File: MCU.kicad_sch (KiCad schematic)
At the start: 0 parts

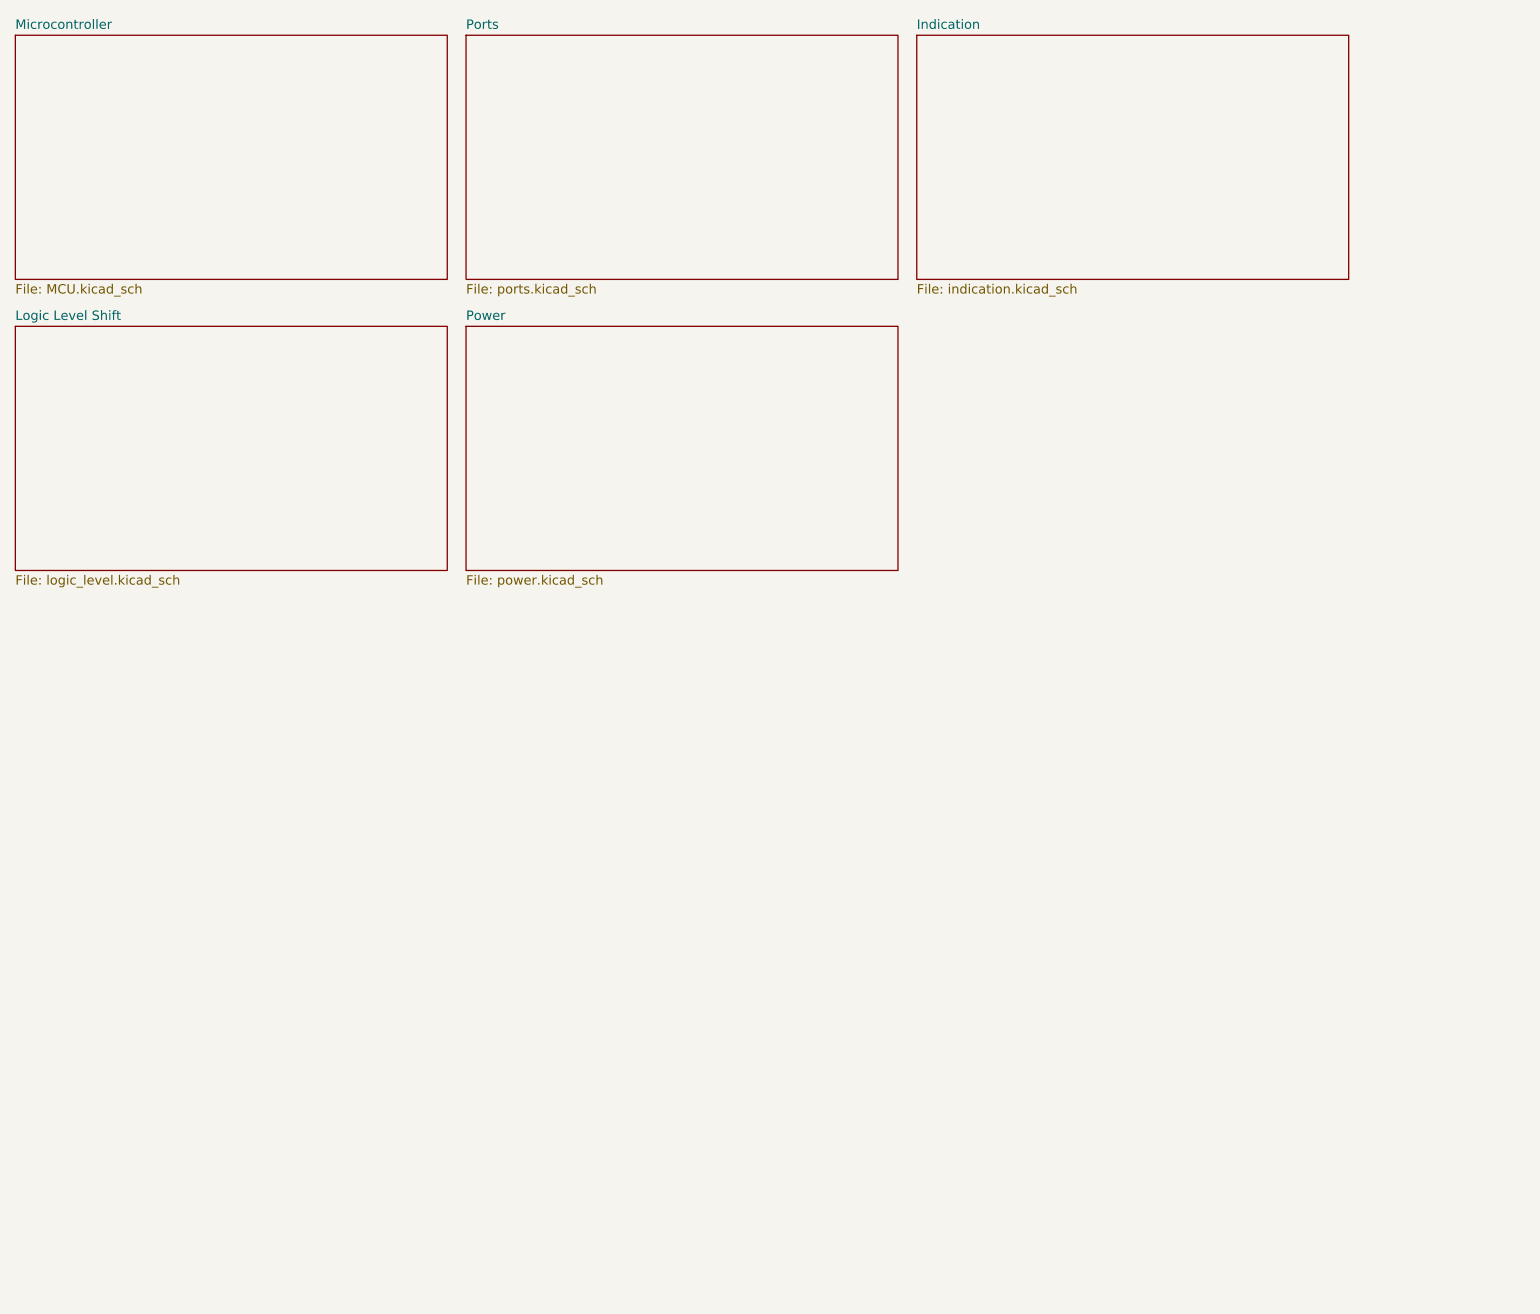
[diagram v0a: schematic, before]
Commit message: Break up schematic into hierarchical sheets
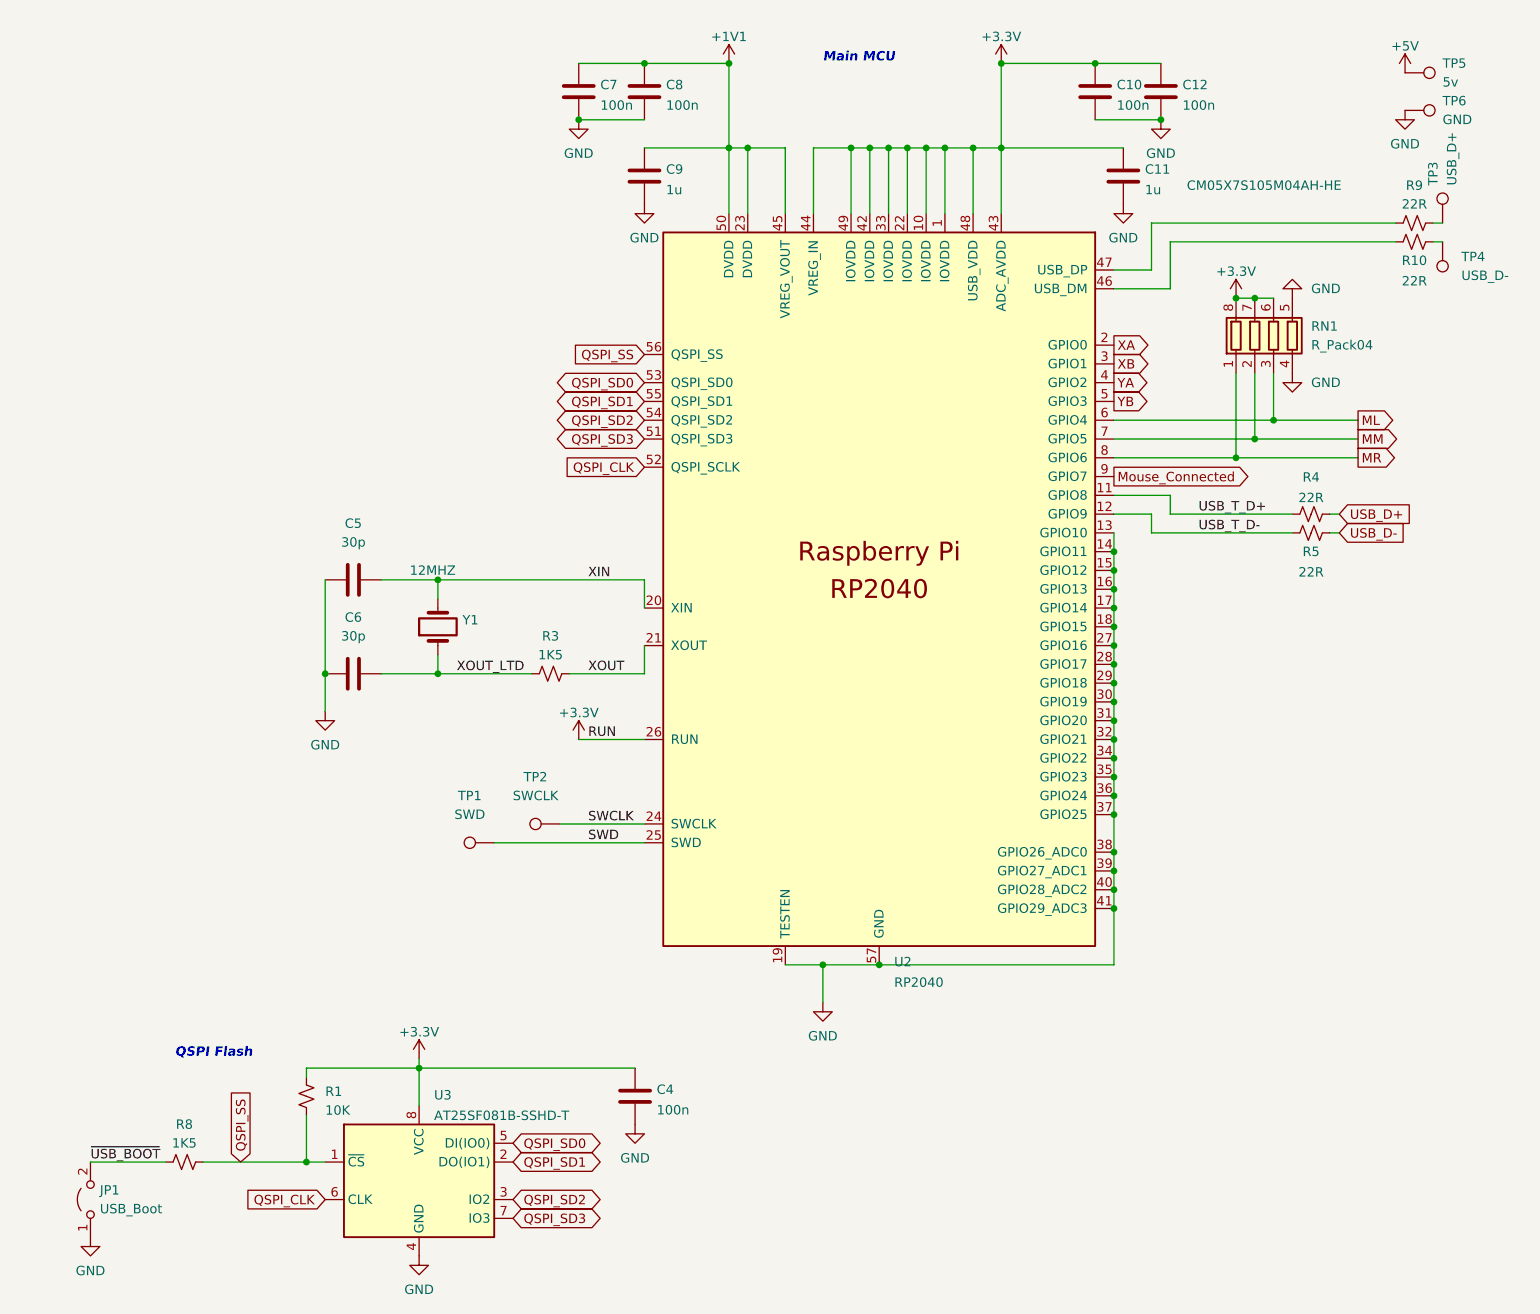
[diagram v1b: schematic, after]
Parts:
- added C10, C12, C4, C7, C8: 100n, Capacitor_SMD:C_0402_1005Metric, symbol Device:C
- added C11, C9: 1u, Capacitor_SMD:C_0402_1005Metric, symbol Device:C
- added C5, C6: 30p, Capacitor_SMD:C_0402_1005Metric, symbol Device:C
- added JP1: USB_Boot, Connector_PinHeader_1.27mm:PinHeader_1x02_P1.27mm_Vertical, symbol Jumper:Jumper_2_Open
- added R1: 10K, Resistor_SMD:R_0402_1005Metric, symbol Device:R_Small_US
- added R10, R4, R5, R9: 22R, Resistor_SMD:R_0402_1005Metric, symbol Device:R_Small_US
- added R3, R8: 1K5, Resistor_SMD:R_0402_1005Metric, symbol Device:R_Small_US
- added RN1: R_Pack04, Resistor_SMD:R_Array_Concave_4x0402, symbol Device:R_Pack04
- added TP1: SWD, TestPoint:TestPoint_Pad_D1.0mm, symbol Connector:TestPoint
- added TP2: SWCLK, TestPoint:TestPoint_Pad_D1.0mm, symbol Connector:TestPoint
- added TP3: USB_D+, TestPoint:TestPoint_Pad_D1.0mm, symbol Connector:TestPoint
- added TP4: USB_D-, TestPoint:TestPoint_Pad_D1.0mm, symbol Connector:TestPoint
- added TP5: 5v, TestPoint:TestPoint_Pad_D1.0mm, symbol Connector:TestPoint
- added TP6: GND, TestPoint:TestPoint_Pad_D1.0mm, symbol Connector:TestPoint
- added U2: RP2040, Library:RP2040-QFN-56, symbol RP2040:RP2040
- added U3: AT25SF081B-SSHD-T, Package_SO:SOIC-8-1EP_3.9x4.9mm_P1.27mm_EP2.29x3mm, symbol Memory_Flash:W25Q32JVZP
- added Y1: 12MHZ, Crystal:Crystal_SMD_5032-2Pin_5.0x3.2mm, symbol Device:Crystal
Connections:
- new net: R10.1, TP4.1
- new net: R10.2, U2.46 (USB_DM)
- new net: R9.2, TP3.1
- new net: R9.1, U2.47 (USB_DP)
- new net +1V1: C7.1, C8.1, C9.1, U2.23 (DVDD), U2.45 (VREG_VOUT), U2.50 (DVDD)
- new net +3V3: C10.1, C11.1, C12.1, C4.1, R1.1, RN1.6 (R3.2), RN1.7 (R2.2), RN1.8 (R1.2), U2.1 (IOVDD), U2.10 (IOVDD), U2.22 (IOVDD), U2.26 (RUN), U2.33 (IOVDD), U2.42 (IOVDD), U2.43 (ADC_AVDD), U2.44 (VREG_IN), U2.48 (USB_VDD), U2.49 (IOVDD), U3.8 (VCC)
- new net +5V: TP5.1
- new net GND: C10.2, C11.2, C12.2, C4.2, C5.1, C6.1, C7.2, C8.2, C9.2, JP1.1 (A), RN1.4 (R4.1), RN1.5 (R4.2), TP6.1, U2.13 (GPIO10), U2.14 (GPIO11), U2.15 (GPIO12), U2.16 (GPIO13), U2.17 (GPIO14), U2.18 (GPIO15), U2.19 (TESTEN), U2.27 (GPIO16), U2.28 (GPIO17), U2.29 (GPIO18), U2.30 (GPIO19), U2.31 (GPIO20), U2.32 (GPIO21), U2.34 (GPIO22), U2.35 (GPIO23), U2.36 (GPIO24), U2.37 (GPIO25), U2.38 (GPIO26_ADC0), U2.39 (GPIO27_ADC1), U2.40 (GPIO28_ADC2), U2.41 (GPIO29_ADC3), U2.57 (GND), U3.4 (GND)
- new net ML: RN1.3 (R3.1), U2.6 (GPIO4)
- new net MM: RN1.2 (R2.1), U2.7 (GPIO5)
- new net MR: RN1.1 (R1.1), U2.8 (GPIO6)
- new net Mouse_Connected: U2.9 (GPIO7)
- new net QSPI_CLK: U2.52 (QSPI_SCLK), U3.6 (CLK)
- new net QSPI_SD0: U2.53 (QSPI_SD0), U3.5 (DI(IO0))
- new net QSPI_SD1: U2.55 (QSPI_SD1), U3.2 (DO(IO1))
- new net QSPI_SD2: U2.54 (QSPI_SD2), U3.3 (IO2)
- new net QSPI_SD3: U2.51 (QSPI_SD3), U3.7 (IO3)
- new net QSPI_SS: R1.2, R8.2, U2.56 (QSPI_SS), U3.1 (~{CS})
- new net SWCLK: TP2.1, U2.24 (SWCLK)
- new net SWD: TP1.1, U2.25 (SWD)
- new net USB_D+: R4.2
- new net USB_D-: R5.1
- new net USB_T_D+: R4.1, U2.11 (GPIO8)
- new net USB_T_D-: R5.2, U2.12 (GPIO9)
- new net XA: U2.2 (GPIO0)
- new net XB: U2.3 (GPIO1)
- new net XIN: C5.2, U2.20 (XIN), Y1.2
- new net XOUT: R3.2, U2.21 (XOUT)
- new net XOUT_LTD: C6.2, R3.1, Y1.1
- new net YA: U2.4 (GPIO2)
- new net YB: U2.5 (GPIO3)
- new net ~{USB_BOOT}: JP1.2 (B), R8.1
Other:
- removed sheet Indication
- removed sheet Logic Level Shift
- removed sheet Microcontroller
- removed sheet Ports
- removed sheet Power
- note added: "Main MCU"
- note added: "QSPI Flash"

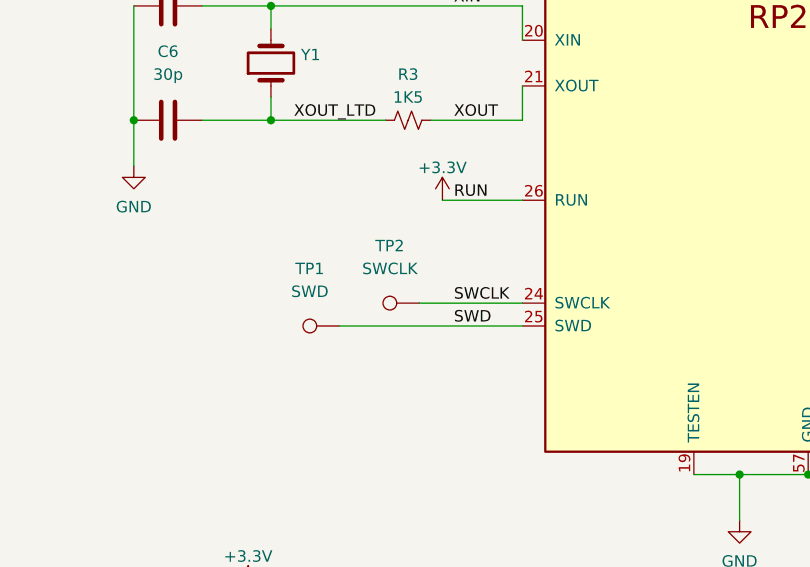
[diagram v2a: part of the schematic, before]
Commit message: Rev 6
Fully rerouted the board to make it cheaper and easier to make at PCBWay
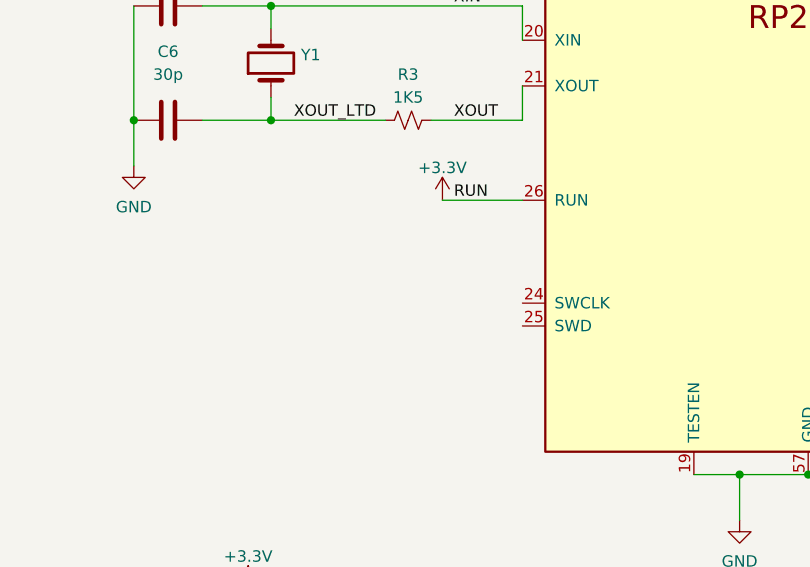
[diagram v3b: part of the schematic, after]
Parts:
- removed TP1: SWD, TestPoint:TestPoint_Pad_D1.0mm, symbol Connector:TestPoint
- removed TP2: SWCLK, TestPoint:TestPoint_Pad_D1.0mm, symbol Connector:TestPoint
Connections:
- net SWCLK: no longer names the net of U2.24 (SWCLK)
- net SWD: no longer names the net of U2.25 (SWD)
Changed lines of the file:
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@@
   (title_block
     (title "RP2040 USB to Quadrature Mouse Adaptor")
-    (date "2023-01-21")
-    (rev "5")
+    (date "2023-02-25")
+    (rev "6")
     (company "Darrens Lab")
   )
@@
     (stroke (width 0) (type default))
   )
-  (wire (pts (xy 102.87 130.81) (xy 114.3 130.81))
-    (stroke (width 0) (type default))
-  )
   (wire (pts (xy 177.8 106.68) (xy 177.8 109.22))
     (stroke (width 0) (type default))
@@
   )
   (wire (pts (xy 177.8 124.46) (xy 177.8 127))
-    (stroke (width 0) (type default))
-  )
-  (wire (pts (xy 93.98 133.35) (xy 114.3 133.35))
     (stroke (width 0) (type default))
   )
@@
     (effects (font (size 1.27 1.27)) (justify left bottom))
   )
-  (label "SWCLK" (at 106.68 130.81 0) (fields_autoplaced)
-    (effects (font (size 1.27 1.27)) (justify left bottom))
-  )
   (label "USB_T_D+" (at 189.23 88.9 0) (fields_autoplaced)
     (effects (font (size 1.27 1.27)) (justify left bottom))
@@
   )
   (label "XOUT" (at 106.68 110.49 0) (fields_autoplaced)
-    (effects (font (size 1.27 1.27)) (justify left bottom))
-  )
-  (label "SWD" (at 106.68 133.35 0) (fields_autoplaced)
     (effects (font (size 1.27 1.27)) (justify left bottom))
   )
@@
         (path "/7272254d-78d5-4f97-a889-dc8c96dd5957/914c070c-80a0-442d-a9ef-87013588aec4"
           (reference "R1") (unit 1)
-        )
-      )
-    )
-  )
-  (symbol (lib_id "Connector:TestPoint") (at 102.87 130.81 90) (unit 1)
-    (in_bom yes) (on_board yes) (dnp no) (fields_autoplaced)
-    (property "Reference" "TP2" (at 99.568 124.46 90)
-      (effects (font (size 1.27 1.27)))
-    )
-    (property "Value" "SWCLK" (at 99.568 127 90)
-      (effects (font (size 1.27 1.27)))
-    )
-    (property "Footprint" "TestPoint:TestPoint_Pad_D1.0mm" (at 102.87 125.73 0)
-      (effects (font (size 1.27 1.27)) hide)
-    )
-    (property "Datasheet" "~" (at 102.87 125.73 0)
-      (effects (font (size 1.27 1.27)) hide)
-    )
-    (pin "1")
-    (instances
-      (project "RP2040_Mouse"
-        (path "/7272254d-78d5-4f97-a889-dc8c96dd5957"
-          (reference "TP2") (unit 1)
-        )
-        (path "/7272254d-78d5-4f97-a889-dc8c96dd5957/914c070c-80a0-442d-a9ef-87013588aec4"
-          (reference "TP2") (unit 1)
         )
       )
@@
         )
       )
-    )
-  )
-  (symbol (lib_id "Connector:TestPoint") (at 93.98 133.35 90) (unit 1)
-    (in_bom yes) (on_board yes) (dnp no) (fields_autoplaced)
-    (property "Reference" "TP1" (at 90.678 127 90)
-      (effects (font (size 1.27 1.27)))
-    )
-    (property "Value" "SWD" (at 90.678 129.54 90)
-      (effects (font (size 1.27 1.27)))
-    )
-    (property "Footprint" "TestPoint:TestPoint_Pad_D1.0mm" (at 93.98 128.27 0)
-      (effects (font (size 1.27 1.27)) hide)
-    )
-    (property "Datasheet" "~" (at 93.98 128.27 0)
-      (effects (font (size 1.27 1.27)) hide)
-    )
-    (pin "1")
-    (instances
-      (project "RP2040_Mouse"
-        (path "/7272254d-78d5-4f97-a889-dc8c96dd5957"
-          (reference "TP1") (unit 1)
-        )
-        (path "/7272254d-78d5-4f97-a889-dc8c96dd5957/914c070c-80a0-442d-a9ef-87013588aec4"
-          (reference "TP1") (unit 1)
-        )
-      )
